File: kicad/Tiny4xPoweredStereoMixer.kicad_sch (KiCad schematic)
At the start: 43 parts, among them J1 AudioJack3_SwitchTR, J2 AudioJack3_SwitchTR, J3 AudioJack3_SwitchTR, J4 AudioJack3_SwitchTR, J9 AudioJack3_SwitchTR, U1 TL072, U2 TL072

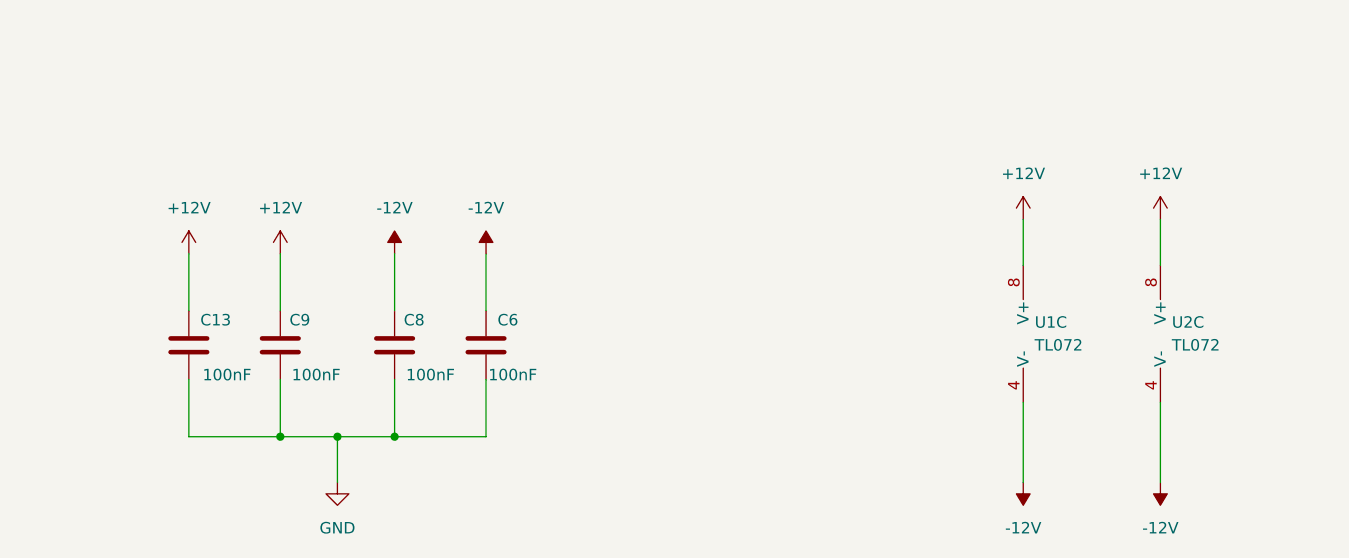
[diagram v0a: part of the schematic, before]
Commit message: changed voltage rails to +/-5V; changed PSU feedback resistor to provide -5V
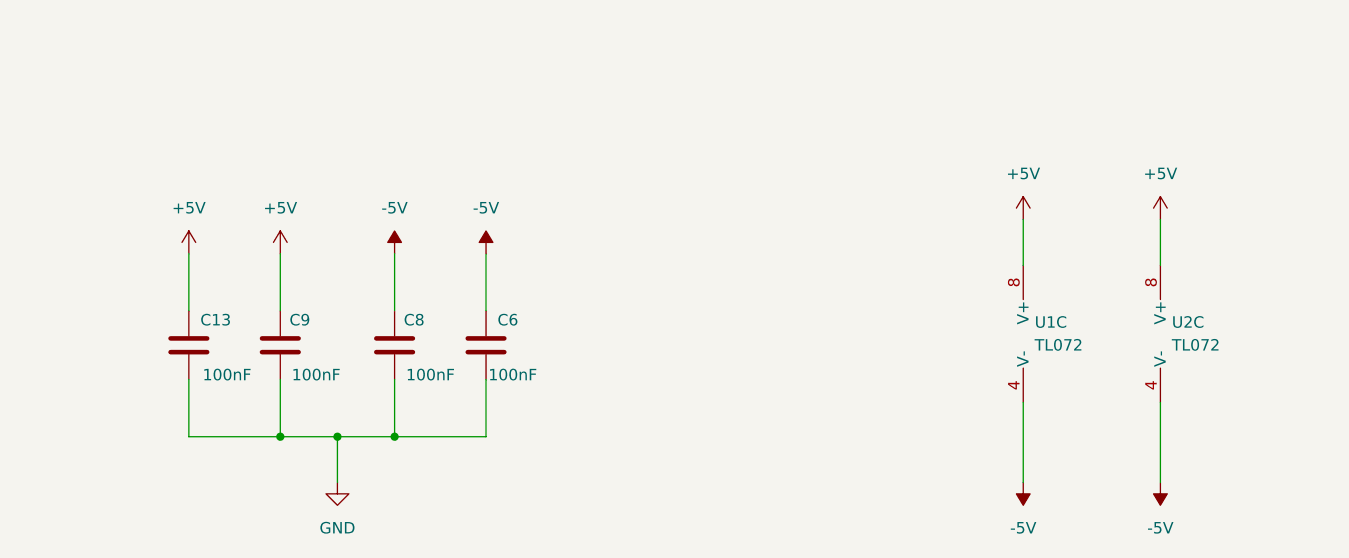
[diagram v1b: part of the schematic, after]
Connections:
- net +12V renamed +5V
- net -12V renamed -5V

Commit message: Revert "changed voltage rails to +/-5V; changed PSU feedback resistor to provide -5V"
This reverts commit 87719da26a309bbde2d2f76146bcb1e510287c62.
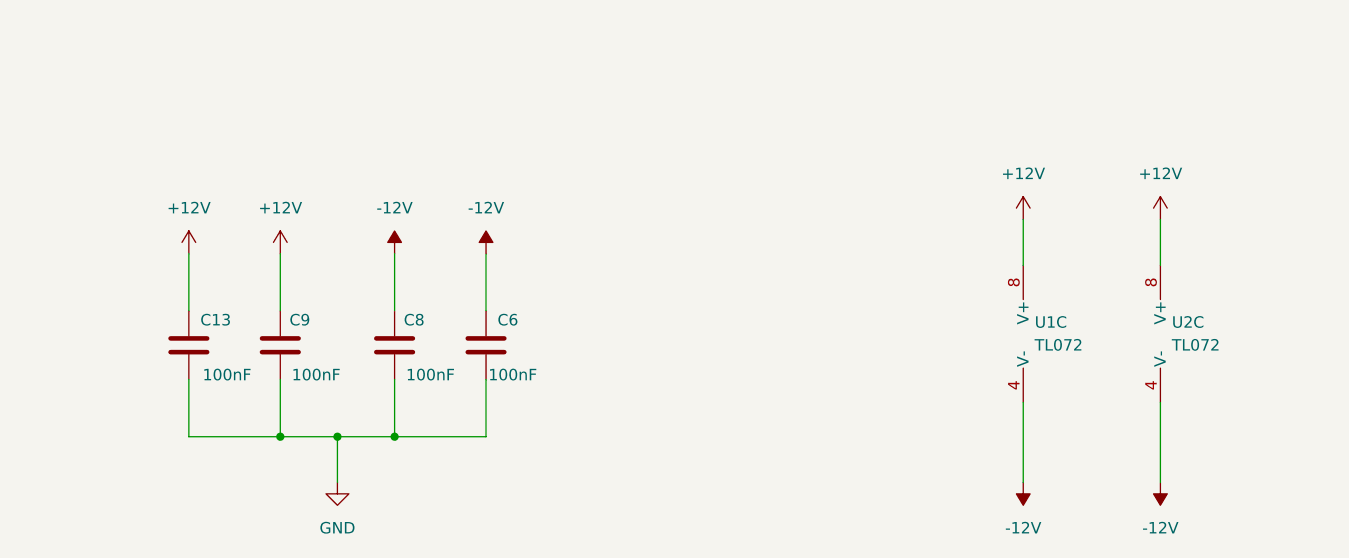
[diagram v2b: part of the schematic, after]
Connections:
- net +5V renamed +12V
- net -5V renamed -12V
